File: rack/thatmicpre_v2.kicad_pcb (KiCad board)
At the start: 2 copper layers, 145.6 x 74.2 mm, 87 parts, among them J1 CON-SOCJ-2155, J2 NC3FBH1, J3 NC3MBH1, J4 Conn_01x03_Female, J5 Conn_01x03_Male, J6 Conn_01x04_Female, J7 Conn_01x04_Male, Q1 BC546CTA, Q2 BC546CTA, SW1 PBH2UEESNPNAGX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

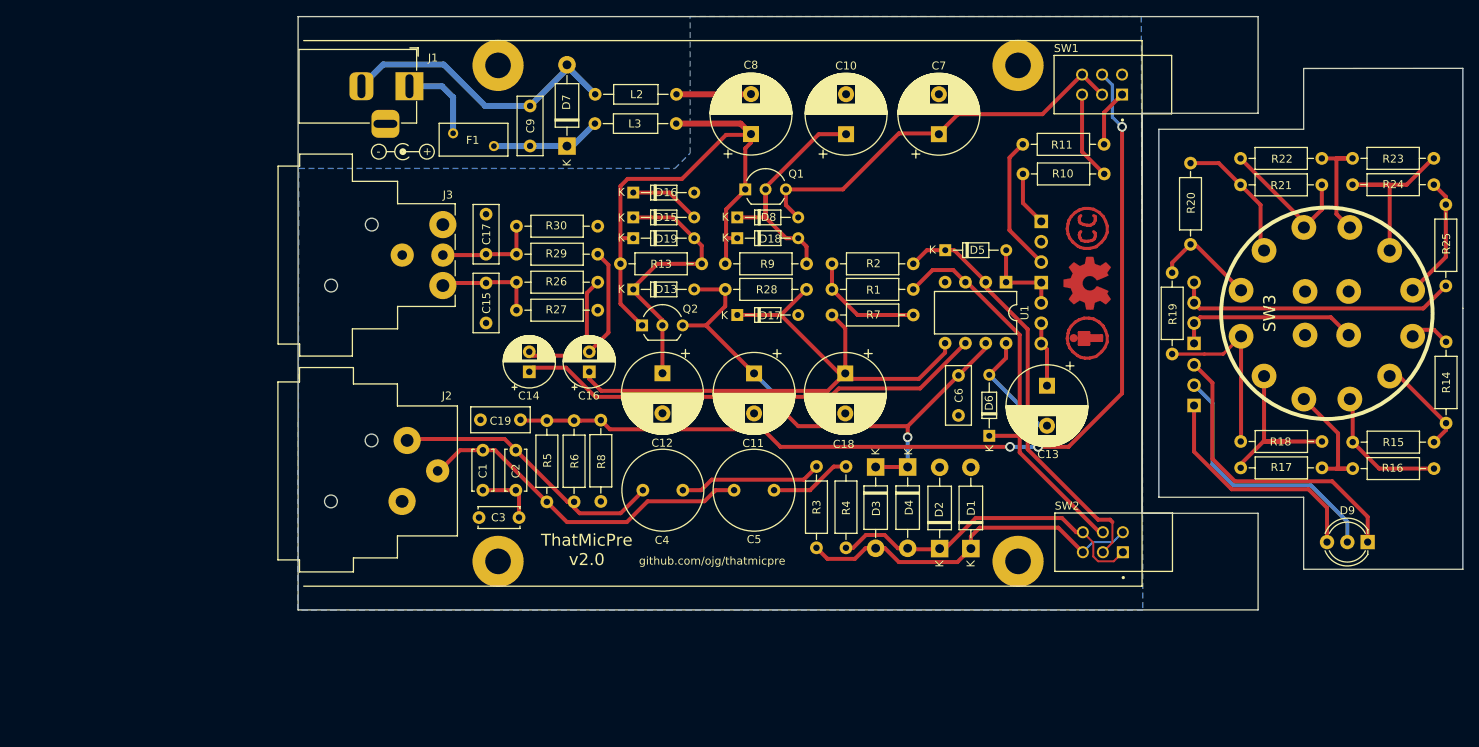
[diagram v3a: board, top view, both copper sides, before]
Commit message: optimized layout
added alternative jack and headers
checked against prints for mech fit
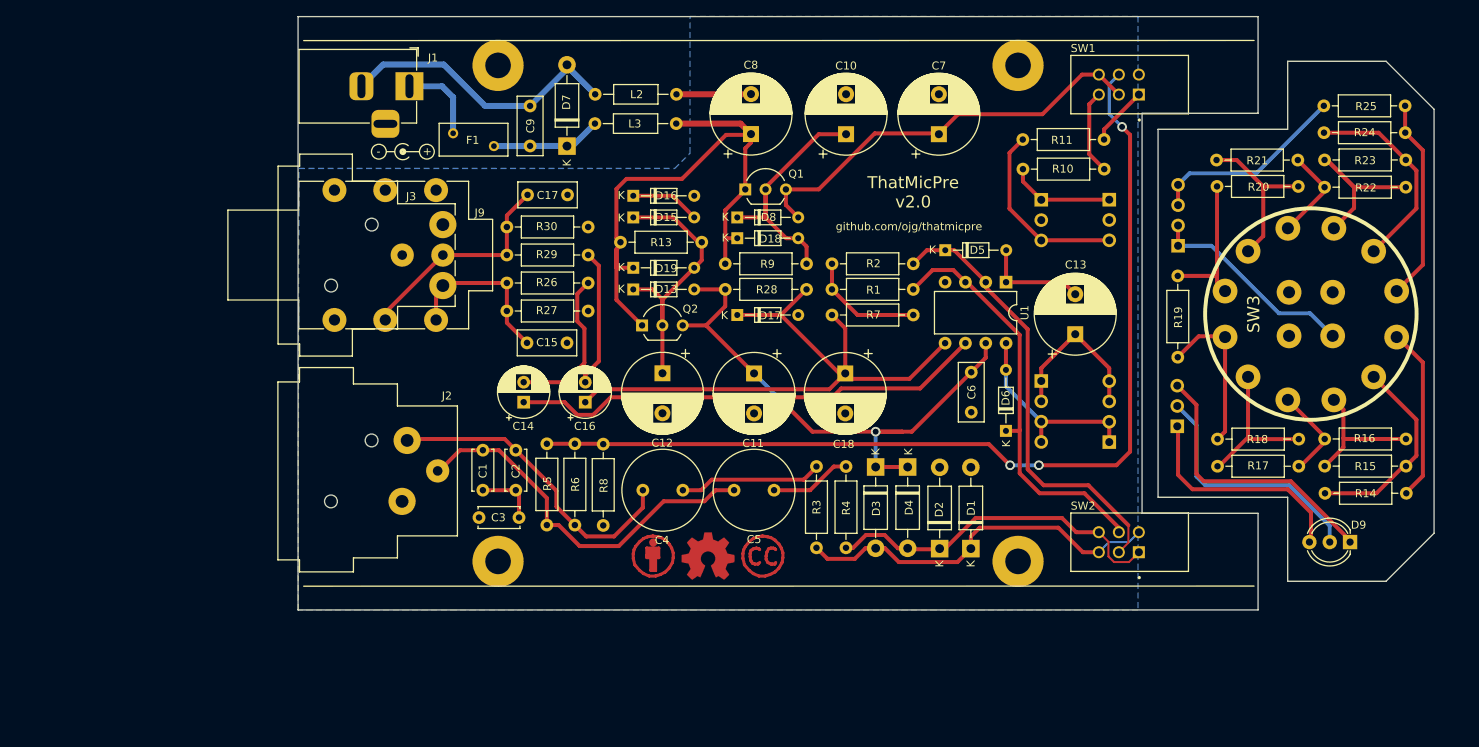
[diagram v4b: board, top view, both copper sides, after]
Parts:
- removed C19: 100n, Capacitor_THT:C_Rect_L7.2mm_W3.0mm_P5.00mm_FKS2_FKP2_MKS2_MKP2
- added J10: Conn_01x03_Female, Connector_PinHeader_2.54mm:PinHeader_1x03_P2.54mm_Vertical, B.Cu at (184.7, 61.1)
- added J8: Conn_01x04_Female, Connector_PinHeader_2.54mm:PinHeader_1x04_P2.54mm_Vertical, B.Cu at (184.7, 91.4)
- added J9: NMJ6HFD2, Connector_Audio:Jack_6.35mm_Neutrik_NMJ6HFD2_Horizontal, F.Cu at (100.5, 76.1)
- moved LOGO2 60.7 mm to (127.7, 105.6), turned to 0 degrees
- moved LOGO1 58.4 mm to (134.5, 105.6), turned to 0 degrees
- moved LOGO3 57.8 mm to (141.3, 105.7), turned to 0 degrees
- moved R14 17.5 mm to (211.7, 97.8), turned to 0 degrees
- moved R20 13.8 mm to (208.3, 59.4), turned to 180 degrees
- moved R25 13.4 mm to (221.7, 49.4), turned to 180 degrees
- moved J7 12.4 mm to (193.3, 66.8)
- moved J6 12.3 mm to (176.2, 83.8)
- moved R22 11.1 mm to (221.8, 59.5)
- moved C15 9.07 mm to (111.9, 79.0), turned to 0 degrees
- moved C17 9.05 mm to (112.0, 60.5), turned to 0 degrees
- moved R24 7.42 mm to (221.7, 52.7)
- moved C13 7.34 mm to (180.4, 77.9), turned to 90 degrees
- moved R16 5.09 mm to (211.6, 91.0)
- moved R15 4.61 mm to (211.6, 94.4)
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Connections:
- C13 pad 2: Net-(C13-Pad2) -> Net-(D5-Pad2)
- D6 pad 2: Net-(C13-Pad2) -> Net-(D6-Pad2)
- J6 pad 1: Net-(D5-Pad2) -> Net-(C13-Pad1)
- J6 pad 2: Net-(D5-Pad2) -> Net-(C13-Pad1)
- J6 pad 3: Net-(C13-Pad1) -> Net-(D6-Pad2)
- J6 pad 4: Net-(C13-Pad1) -> Net-(D6-Pad2)
- U1 pad 8: Net-(C13-Pad2) -> Net-(D6-Pad2)
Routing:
- net Net-(D6-Pad2): track 0.00 -> 25.2 mm
- net Net-(R14-Pad2): track 5.13 -> 21.8 mm
- net Net-(C17-Pad1): track 12.7 -> 27.6 mm
- net Net-(C13-Pad2): track 14.7 -> 0.00 mm
- net Net-(R14-Pad1): track 12.5 -> 25.5 mm
- net Net-(C13-Pad1): track 8.11 -> 20.3 mm
- net Net-(J7-Pad3): track 35.5 -> 24.9 mm
- net Net-(R24-Pad1): track 15.5 -> 25.4 mm
- net Net-(C15-Pad1): track 12.9 -> 21.3 mm
- net Net-(R22-Pad1): track 16.2 -> 23.0 mm
- net Net-(J4-Pad3): track 17.0 -> 23.5 mm
- net Net-(J4-Pad1): track 6.88 -> 13.3 mm
- net Net-(R21-Pad1): track 18.2 -> 11.8 mm
- net Net-(R19-Pad1): track 13.2 -> 19.5 mm
- net Net-(R16-Pad1): track 16.7 -> 11.7 mm
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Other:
- board size 145.6 x 74.2 mm -> 142 x 74.2 mm

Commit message: Production version of v2.0 (rack version) with panels
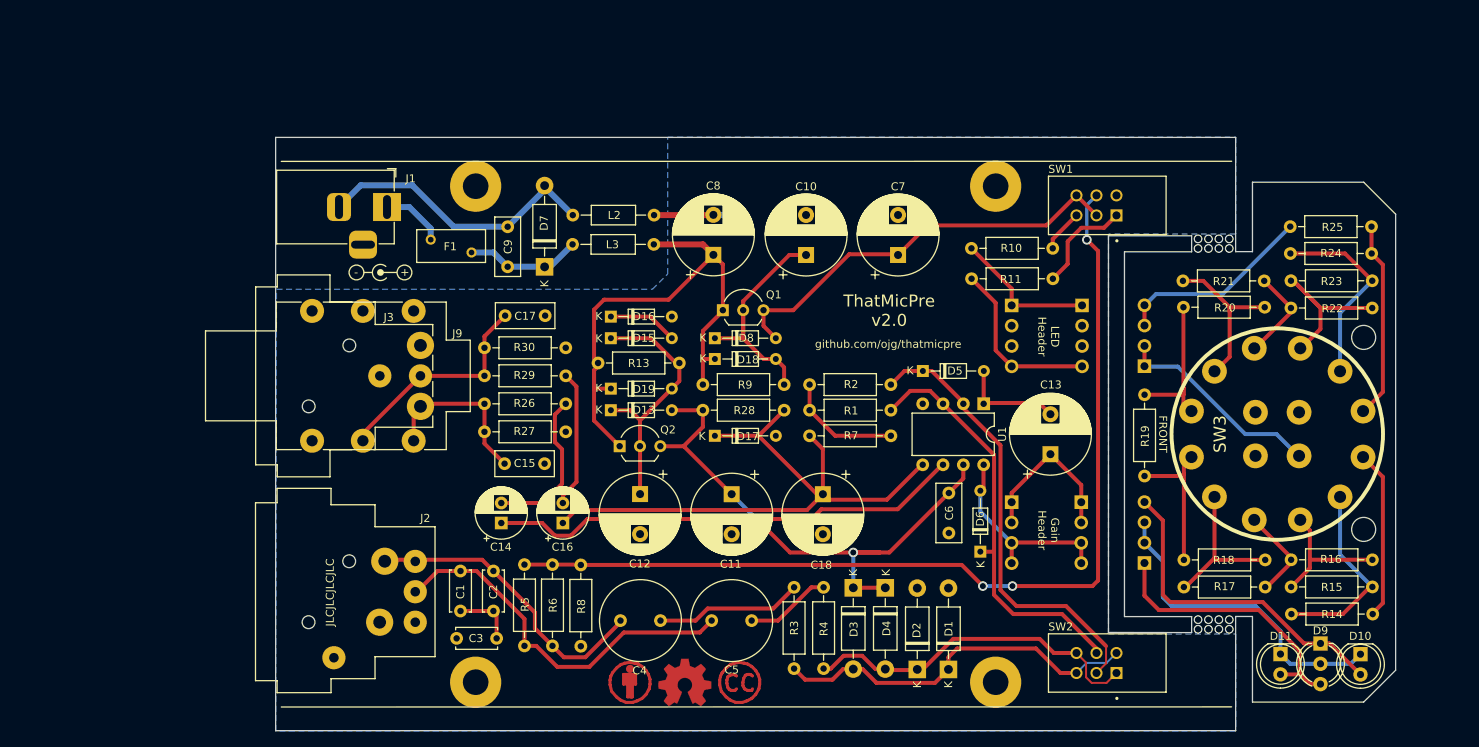
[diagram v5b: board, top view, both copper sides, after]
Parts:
- added ?: , , F.Cu at (98.0, 106.3)
- added ?: , , F.Cu at (97.9, 113.9)
- added D10: LED, LED_THT:LED_D5.0mm, F.Cu at (216.1, 117.9)
- added D11: LED, LED_THT:LED_D5.0mm, F.Cu at (206.1, 117.9)
- J10: value Conn_01x03_Female -> Angled pinheader; footprint Connector_PinHeader_2.54mm:PinHeader_1x03_P2.54mm_Vertical -> Connector_PinHeader_2.54mm:PinHeader_1x04_P2.54mm_Vertical
- J2: value NC3FBH1 -> NC3FBH2; footprint Connector_Audio:Jack_XLR_Neutrik_NC3FBH1_Horizontal -> Connector_Audio:Jack_XLR_Neutrik_NC3FBH2_Horizontal
- J4: value Conn_01x03_Female -> Female header; footprint Connector_PinSocket_2.54mm:PinSocket_1x03_P2.54mm_Horizontal -> Connector_PinSocket_2.54mm:PinSocket_1x04_P2.54mm_Horizontal
- J5: value Conn_01x03_Male -> Male pinheader; footprint Connector_PinHeader_2.54mm:PinHeader_1x03_P2.54mm_Vertical -> Connector_PinHeader_2.54mm:PinHeader_1x04_P2.54mm_Vertical
- J6: value Conn_01x04_Female -> Female header
- J7: value Conn_01x04_Male -> Male pinheader
- J8: value Conn_01x04_Female -> Angled pinheader
- R27, R30: value 10k -> 47k
- SW1, SW2: value PBH2UEESNPNAGX -> DPDT
- moved R11 18.5 mm to (177.7, 71.0)
- moved J5 17.6 mm to (189.1, 106.5)
- moved C4 16.5 mm to (123.6, 113.7)
- moved C5 16.5 mm to (135.0, 113.7)
- moved LOGO2 16.1 mm to (124.8, 121.4)
- moved LOGO3 16.1 mm to (138.4, 121.5)
- moved LOGO1 16.1 mm to (131.6, 121.4)
- moved C7 15.9 mm to (158.3, 68.0)
- moved C10 15.9 mm to (146.8, 68.0)
- moved C8 15.8 mm to (135.2, 68.0)
- moved R21 15.7 mm to (204.1, 71.2)
- moved R23 15.7 mm to (217.6, 71.2)
- moved R16 15.7 mm to (207.4, 106.1)
- moved R18 15.7 mm to (194.0, 106.1)
- moved R20 15.7 mm to (204.1, 74.5)
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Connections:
- J10 pad 3: Net-(J4-Pad3) -> GND
- J3 pad G: (no net) -> GND
- J4 pad 3: Net-(J4-Pad3) -> GND
- J5 pad 3: Net-(D9-Pad1) -> Net-(D9-Pad2)
- J8 pad 1: Net-(D6-Pad2) -> Net-(C13-Pad1)
- J8 pad 2: Net-(D6-Pad2) -> Net-(C13-Pad1)
- J8 pad 3: Net-(C13-Pad1) -> Net-(D6-Pad2)
- J8 pad 4: Net-(C13-Pad1) -> Net-(D6-Pad2)
- R11 pad 2: Net-(J4-Pad3) -> Net-(R11-Pad2)
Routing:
- net Net-(J4-Pad3): track 23.5 -> 0.00 mm
- net Net-(R11-Pad2): track 0.00 -> 22.2 mm
- net Net-(D9-Pad2): track 31.1 -> 40.6 mm
- net Net-(D9-Pad3): track 28.5 -> 36.5 mm
- net Net-(D9-Pad1): track 34.9 -> 41.4 mm
- net Net-(R11-Pad1): track 7.42 -> 12.9 mm
- net Net-(R10-Pad1): track 10.6 -> 5.35 mm
- net Net-(J4-Pad1): track 13.3 -> 18.0 mm
- net /VIN: track 71.8 -> 68.2 mm
- net Net-(F1-Pad1): track 10.5 -> 7.97 mm
- net Net-(R18-Pad1): track 20.2 -> 18.3 mm
- net Net-(C10-Pad1): track 32.4 -> 30.7 mm
- net Net-(C2-Pad1): track 39.5 -> 37.8 mm
- net Net-(R23-Pad1): track 25.8 -> 24.6 mm
- net Net-(R5-Pad1): track 123.4 -> 122.3 mm
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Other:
- board size 142 x 74.2 mm -> 140 x 74.2 mm
- board text added: "BACK"
- board text added: "FRONT"
- board text added: "Gain Header"
- board text added: "JLCJLCJLCJLC"
- board text added: "LED Header"

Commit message: Modified rack version BOM to match assembled prototype
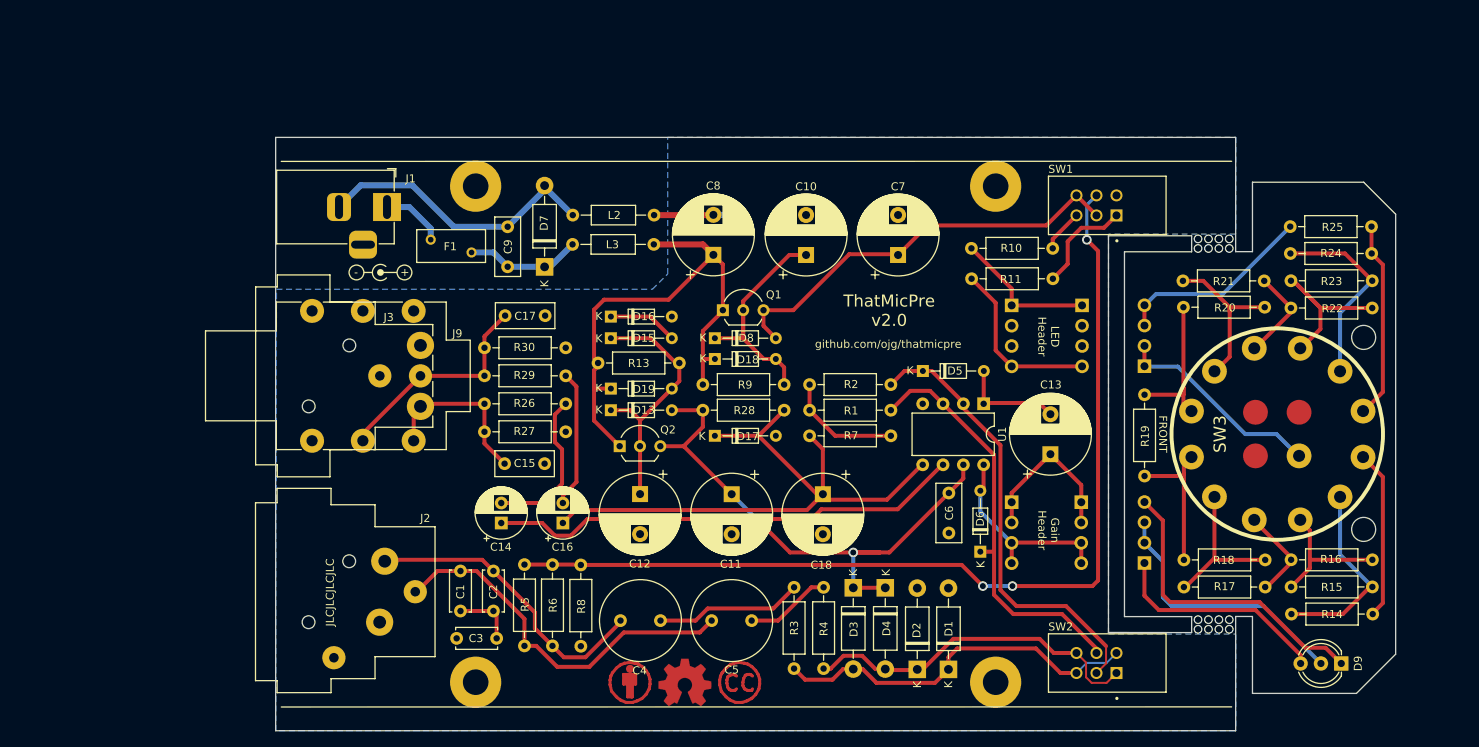
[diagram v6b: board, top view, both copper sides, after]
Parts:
- removed ? (x2): , 
- removed D10, D11: LED, LED_THT:LED_D5.0mm
- C14, C16: value 22u-63V -> 22u-50V
- C18: value 1000u-25V -> 220u-63V
- D15, D16, D17: value 18V -> 16V
- L2, L3: value 4u7 -> 10u
- R14: value 1M0 -> 8K06
- R15: value 2k7 -> 909R
- R16: value 1k0 -> 453R
- R17: value 560R -> 237R
- R18: value 270R -> 127R
- R19: value 150R -> 71R
- R20: value 82R -> 39R
- R21: value 47R -> 22R
- R22: value 27R -> 12R4
- R23: value 15R -> 6R81
- R24: value 8R2 -> 3R9
- R25: value 10R -> 4R99
- U1: value THAT1510P08-U -> 1512P08-U
- moved D9 3.61 mm to (213.7, 119.1), turned to 180 degrees
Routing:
- net Net-(D9-Pad3): track 36.5 -> 27.7 mm
- net Net-(D9-Pad2): track 40.6 -> 33.4 mm
- net Net-(D9-Pad1): track 41.4 -> 38.4 mm
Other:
- outline, holes or cut-outs redrawn
